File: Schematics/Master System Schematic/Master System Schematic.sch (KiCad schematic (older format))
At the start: 27 parts, among them J1 GND, J2 TS+, J3 TS-, SW1 GLVMS, SW2 SideMounted (BRB), SW3 SideMounted (BRB)

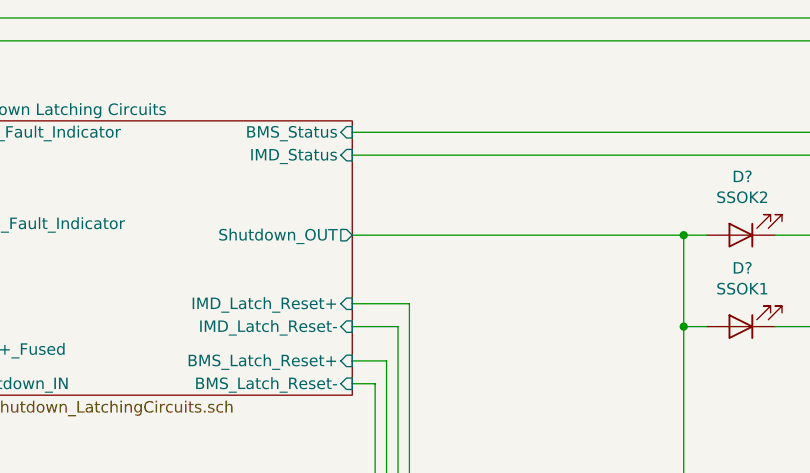
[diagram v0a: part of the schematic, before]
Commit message: Adding ground pin to fault pcb enclosure
Needed ground pin for fault pcb enclosure
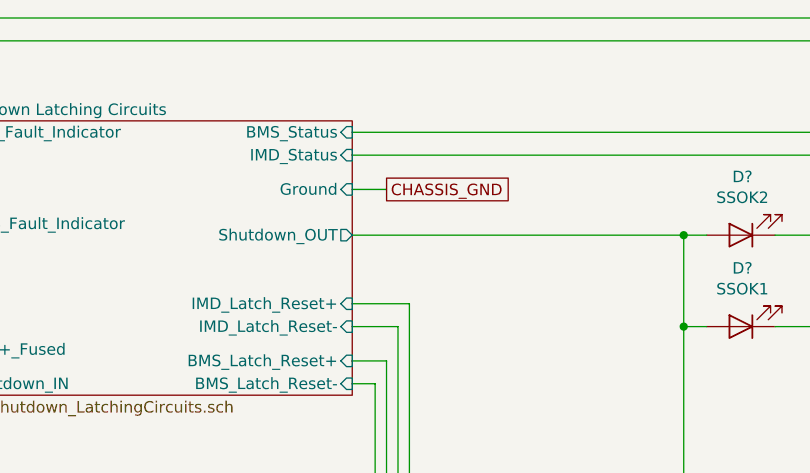
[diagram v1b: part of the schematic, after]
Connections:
- wire segments 140 -> 141
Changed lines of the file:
@@
 F11 "BMS_Latch_Reset+" I R 4700 2500 50
 F12 "BMS_Latch_Reset-" I R 4700 2600 50
+F13 "Ground" I R 4700 1750 50
 $EndSheet
 $Comp
@@
 Wire Wire Line
 	6150 5100 6150 5500
+Text GLabel 4850 1750 2    50   UnSpc ~ 0
+CHASSIS_GND
+Wire Wire Line
+	4850 1750 4700 1750
 $EndSCHEMATC

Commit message: Updated shutdown circuit to reflect changes
>updated latching circuit design to be 4 DPDT relays
>updated reset switch design to be dpst button to actuate both latches simultaneously
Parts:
- removed SW?: IMD_FaultLatch_Reset, symbol Switch:SW_Push
- removed SW?: BMS_FaultLatch_Reset, symbol Switch:SW_Push
- added SW?: Latching Circuit Reset [Momentary Button NO], symbol Switch:SW_DPST
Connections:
- wire segments 141 -> 145
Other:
- moved on the sheet: J1, J2, J3
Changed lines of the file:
@@
 F3 "Shutdown_IN" I L 2950 2600 50
 F4 "IMD_Fault_Indicator" O L 2950 1500 50
-F5 "IMD_Latch_Reset+" I R 4700 2250 50
-F6 "IMD_Latch_Reset-" I R 4700 2350 50
+F5 "IMD_Latch_Reset+" I R 4700 2400 50
+F6 "IMD_Latch_Reset-" I R 4700 2500 50
 F7 "GLV+_Fused" I L 2950 2450 50
 F8 "IMD_Status" I R 4700 1600 50
 F9 "BMS_Status" I R 4700 1500 50
 F10 "BMS_Fault_Indicator" O L 2950 1900 50
-F11 "BMS_Latch_Reset+" I R 4700 2500 50
+F11 "BMS_Latch_Reset+" I R 4700 2300 50
 F12 "BMS_Latch_Reset-" I R 4700 2600 50
 F13 "Ground" I R 4700 1750 50
@@
 L Connector:Conn_01x01_Female J3
 U 1 1 5FB0713A
-P 5550 7950
-F 0 "J3" V 5450 7800 50  0000 L CNN
-F 1 "TS-" V 5350 7750 50  0000 L CNN
-F 2 "" H 5550 7950 50  0001 C CNN
-F 3 "~" H 5550 7950 50  0001 C CNN
-	1    5550 7950
+P 5850 8650
+F 0 "J3" V 5750 8500 50  0000 L CNN
+F 1 "TS-" V 5650 8450 50  0000 L CNN
+F 2 "" H 5850 8650 50  0001 C CNN
+F 3 "~" H 5850 8650 50  0001 C CNN
+	1    5850 8650
 	0    -1   1    0
 $EndComp
@@
 L Connector:Conn_01x01_Female J2
 U 1 1 5FB022E4
-P 5300 7950
-F 0 "J2" V 5200 7800 50  0000 L CNN
-F 1 "TS+" V 5100 7750 50  0000 L CNN
-F 2 "" H 5300 7950 50  0001 C CNN
-F 3 "~" H 5300 7950 50  0001 C CNN
-	1    5300 7950
+P 5600 8650
+F 0 "J2" V 5500 8500 50  0000 L CNN
+F 1 "TS+" V 5400 8450 50  0000 L CNN
+F 2 "" H 5600 8650 50  0001 C CNN
+F 3 "~" H 5600 8650 50  0001 C CNN
+	1    5600 8650
 	0    -1   1    0
 $EndComp
@@
 L Connector:Conn_01x01_Female J1
 U 1 1 5FAE402D
-P 5050 7950
-F 0 "J1" V 4950 7800 50  0000 L CNN
-F 1 "GND" V 4850 7750 50  0000 L CNN
-F 2 "" H 5050 7950 50  0001 C CNN
-F 3 "~" H 5050 7950 50  0001 C CNN
-	1    5050 7950
+P 6100 8650
+F 0 "J1" V 6000 8500 50  0000 L CNN
+F 1 "GND" V 5900 8450 50  0000 L CNN
+F 2 "" H 6100 8650 50  0001 C CNN
+F 3 "~" H 6100 8650 50  0001 C CNN
+	1    6100 8650
 	0    -1   1    0
 $EndComp
-Text Notes 3850 8200 0    50   ~ 0
+Text Notes 4400 8900 0    50   ~ 0
 TSMP and Shutdown Reset Container
 Text GLabel 6150 5600 0    50   UnSpc ~ 0
@@
 F18 "Segment4_VoltageTaps" I L 10100 6850 50
 $EndSheet
-Text GLabel 5150 6750 2    50   UnSpc ~ 0
+Text GLabel 6450 8050 2    50   UnSpc ~ 0
 CHASSIS_GND
 $Comp
@@
 Wire Wire Line
 	1850 1000 1850 3350
-$Comp
-L Switch:SW_Push SW?
-U 1 1 5FA44CBD
-P 4400 7700
-F 0 "SW?" H 4400 7850 50  0000 C CNN
-F 1 "IMD_FaultLatch_Reset" H 4400 7950 50  0000 C CNN
-F 2 "" H 4400 7900 50  0001 C CNN
-F 3 "https://www.mouser.com/datasheet/2/57/Bulgin_2010_p194-10070.pdf" H 4400 7900 50  0001 C CNN
-	1    4400 7700
-	-1   0    0    1
-$EndComp
-$Comp
-L Switch:SW_Push SW?
-U 1 1 5FA470C6
-P 4400 7150
-F 0 "SW?" H 4400 7300 50  0000 C CNN
-F 1 "BMS_FaultLatch_Reset" H 4400 7400 50  0000 C CNN
-F 2 "" H 4400 7350 50  0001 C CNN
-F 3 "https://www.mouser.com/datasheet/2/57/Bulgin_2010_p194-10070.pdf" H 4400 7350 50  0001 C CNN
-	1    4400 7150
-	-1   0    0    1
-$EndComp
 Wire Wire Line
 	6150 5500 6700 5500
@@
 	6150 1950 6250 1950
 Wire Wire Line
-	4600 7700 4950 7700
-Wire Wire Line
-	4200 7700 4000 7700
-Wire Wire Line
-	4000 7700 4000 7600
-Wire Wire Line
-	4000 7600 4900 7600
-Wire Wire Line
-	4200 7150 4000 7150
-Wire Wire Line
-	4000 7150 4000 7050
-Wire Wire Line
-	4600 7150 4850 7150
-Wire Wire Line
-	4000 7050 4800 7050
-Wire Wire Line
-	4800 2600 4700 2600
-Wire Wire Line
-	4700 2500 4850 2500
-Wire Wire Line
-	4900 2350 4700 2350
-Wire Wire Line
-	4700 2250 4950 2250
-Wire Wire Line
 	6150 2350 6150 3150
 Connection ~ 6150 2350
@@
 	6150 4400 6150 3550
 Wire Notes Line
-	3800 8050 3800 6850
+	4350 8750 4350 7550
 Wire Notes Line
-	3800 6850 5850 6850
+	4350 7550 6400 7550
 Wire Notes Line
-	5850 6850 5850 8050
+	6400 7550 6400 8750
 Wire Notes Line
-	5850 8050 3800 8050
+	6400 8750 4350 8750
 Wire Wire Line
 	11500 6100 11700 6100
@@
 $EndComp
 Wire Wire Line
-	5150 6750 5050 6750
-Wire Wire Line
-	5300 7100 6700 7100
-Wire Wire Line
-	5550 7200 6700 7200
-Wire Wire Line
-	4800 2600 4800 7050
-Wire Wire Line
-	4850 2500 4850 7150
-Wire Wire Line
-	4900 2350 4900 7600
-Wire Wire Line
-	4950 2250 4950 7700
-Wire Wire Line
 	1850 3950 6900 3950
 Wire Wire Line
@@
 Wire Wire Line
 	2300 2600 2300 3000
-Wire Wire Line
-	5050 6750 5050 7750
-Wire Wire Line
-	5300 7100 5300 7750
-Wire Wire Line
-	5550 7200 5550 7750
 Connection ~ 6150 5100
 Wire Wire Line
@@
 Wire Wire Line
 	4850 1750 4700 1750
+Wire Wire Line
+	4750 8150 4700 8150
+Wire Wire Line
+	4700 8150 4700 8050
+Wire Wire Line
+	4700 8050 4900 8050
+Wire Wire Line
+	5150 8150 5200 8150
+Wire Wire Line
+	5200 8150 5200 8050
+Wire Wire Line
+	5200 8050 5000 8050
+Wire Wire Line
+	5150 8350 5250 8350
+Wire Wire Line
+	5250 8350 5250 8000
+Wire Wire Line
+	5250 8000 5050 8000
+Wire Wire Line
+	4750 8350 4650 8350
+Wire Wire Line
+	4650 8350 4650 8000
+Wire Wire Line
+	4650 8000 4850 8000
+Wire Wire Line
+	4850 2600 4850 8000
+Wire Wire Line
+	5050 2300 4700 2300
+Wire Wire Line
+	4700 2600 4850 2600
+Wire Wire Line
+	5050 2300 5050 8000
+Wire Wire Line
+	4700 2400 5000 2400
+Wire Wire Line
+	5000 2400 5000 8050
+Wire Wire Line
+	4900 2500 4700 2500
+Wire Wire Line
+	4900 2500 4900 8050
+Wire Wire Line
+	6700 7100 5600 7100
+Wire Wire Line
+	5600 7100 5600 8450
+Wire Wire Line
+	5850 7200 6700 7200
+Wire Wire Line
+	5850 7200 5850 8450
+Wire Wire Line
+	6450 8050 6100 8050
+Wire Wire Line
+	6100 8050 6100 8450
+$Comp
+L Switch:SW_DPST SW?
+U 1 1 5F864268
+P 4950 8250
+F 0 "SW?" H 4950 8050 50  0000 C CNN
+F 1 "Latching Circuit Reset [Momentary Button NO]" H 4500 7900 50  0000 C CNN
+F 2 "" H 4950 8250 50  0001 C CNN
+F 3 "~" H 4950 8250 50  0001 C CNN
+	1    4950 8250
+	1    0    0    -1
+$EndComp
 $EndSCHEMATC

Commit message: Add CAN Bus Module to Pedal Box
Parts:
- added A1: Arduino_UNO_rev3, symbol NER:Arduino_UNO_rev3
- added R? (x2): R, symbol Device:R
- added U1: CAN_Module, symbol NER:CAN-Module
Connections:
- net labels added: CAN_H, CAN_L, GLV+, GLV_GND, POT1+, POT1-, POT1_INPUT, POT2+, POT2-, POT2_INPUT, Switch1-, Switch2-, Switch_Input1, Switch_Input2
- wire segments 145 -> 205
- no-connect marks 0 -> 26
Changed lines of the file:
@@
 $Descr B 17000 11000
 encoding utf-8
-Sheet 1 11
+Sheet 1 12
 Title "NER FH 2020-2021 Master Electrical Schematic"
 Date "2020-09-17"
@@
 $EndComp
 Wire Wire Line
-	1850 3950 6900 3950
-Wire Wire Line
 	4700 1950 6150 1950
 Wire Wire Line
@@
 	2300 2600 2300 3000
 Connection ~ 6150 5100
-Wire Wire Line
-	6150 5100 6150 5500
 Text GLabel 4850 1750 2    50   UnSpc ~ 0
 CHASSIS_GND
@@
 	1    0    0    -1
 $EndComp
+Text HLabel 6600 3050 2    50   Input ~ 0
+GLV+
+Wire Wire Line
+	6600 3050 5550 3050
+Text HLabel 3600 3050 0    50   Input ~ 0
+GLV_GND
+Wire Wire Line
+	3600 3050 4350 3050
+$Comp
+L NER:Arduino_UNO_rev3 A1
+U 1 1 5F6833F8
+P 4950 2900
+F 0 "A1" H 4950 3015 50  0000 C CNN
+F 1 "Arduino_UNO_rev3" H 4950 2924 50  0000 C CNN
+F 2 "" H 4950 3050 50  0001 C CNN
+F 3 "" H 4950 3050 50  0001 C CNN
+	1    4950 2900
+	1    0    0    -1
+$EndComp
+$Comp
+L NER:CAN-Module U1
+U 1 1 5F6A22C3
+P 7600 3100
+F 0 "U1" H 7625 3115 50  0000 C CNN
+F 1 "CAN_Module" H 7625 3024 50  0000 C CNN
+F 2 "" H 7600 3100 50  0001 C CNN
+F 3 "" H 7600 3100 50  0001 C CNN
+	1    7600 3100
+	1    0    0    -1
+$EndComp
+Wire Wire Line
+	7050 3450 5900 3450
+Wire Wire Line
+	5900 3450 5900 3650
+Wire Wire Line
+	5900 3650 5550 3650
+Wire Wire Line
+	7050 3550 6100 3550
+Wire Wire Line
+	6100 3550 6100 3850
+Wire Wire Line
+	6100 3850 5550 3850
+Wire Wire Line
+	7050 3650 6250 3650
+Wire Wire Line
+	6250 3650 6250 3750
+Wire Wire Line
+	6250 3750 5550 3750
+Wire Wire Line
+	7050 3750 6350 3750
+Wire Wire Line
+	6350 3750 6350 3950
+Wire Wire Line
+	7050 3850 6600 3850
+Wire Wire Line
+	6600 3850 6600 3400
+Wire Wire Line
+	6600 3400 5750 3400
+Wire Wire Line
+	5750 3400 5750 3550
+Wire Wire Line
+	5750 3550 5550 3550
+Text HLabel 8950 3650 2    50   Input ~ 0
+CAN_L
+Text HLabel 8950 3500 2    50   Input ~ 0
+CAN_H
+Wire Wire Line
+	8200 3500 8600 3500
+Wire Wire Line
+	8950 3650 8200 3650
+NoConn ~ 4350 3200
+NoConn ~ 4350 3300
+NoConn ~ 4350 3400
+NoConn ~ 4350 3500
+Wire Wire Line
+	5550 4700 5900 4700
+Wire Wire Line
+	5900 4700 5900 4900
+Connection ~ 5900 4700
+$Comp
+L Device:R R?
+U 1 1 5F71A5F5
+P 5900 5050
+F 0 "R?" H 5970 5096 50  0000 L CNN
+F 1 "R" H 5970 5005 50  0000 L CNN
+F 2 "" V 5830 5050 50  0001 C CNN
+F 3 "~" H 5900 5050 50  0001 C CNN
+	1    5900 5050
+	1    0    0    -1
+$EndComp
+$Comp
+L Device:R R?
+U 1 1 5F71A986
+P 6150 5050
+F 0 "R?" H 6220 5096 50  0000 L CNN
+F 1 "R" H 6220 5005 50  0000 L CNN
+F 2 "" V 6080 5050 50  0001 C CNN
+F 3 "~" H 6150 5050 50  0001 C CNN
+	1    6150 5050
+	1    0    0    -1
+$EndComp
+Wire Wire Line
+	5900 5200 5900 5400
+Wire Wire Line
+	5900 5400 6000 5400
+NoConn ~ 7050 3350
+NoConn ~ 5550 3250
+NoConn ~ 5550 3350
+NoConn ~ 5550 3450
+NoConn ~ 4350 3650
+NoConn ~ 4350 3750
+NoConn ~ 4350 3850
+NoConn ~ 4350 3950
+NoConn ~ 4350 4350
+NoConn ~ 4350 4700
+NoConn ~ 4350 4800
+NoConn ~ 4350 4900
+NoConn ~ 4350 5000
+NoConn ~ 5550 5000
+NoConn ~ 5550 4900
+NoConn ~ 5550 4600
+NoConn ~ 5550 4500
+NoConn ~ 5550 4400
+NoConn ~ 5550 4300
+NoConn ~ 5550 4150
+NoConn ~ 5550 4050
+Text HLabel 6800 4700 2    50   Input ~ 0
+Switch_Input1
+Text HLabel 6800 5050 2    50   Input ~ 0
+Switch_Input2
+Wire Wire Line
+	4350 4250 3950 4250
+Wire Wire Line
+	3950 4250 3950 4600
+Wire Wire Line
+	3950 5650 6000 5650
+Wire Wire Line
+	6600 5650 6600 5150
+Wire Wire Line
+	6600 4600 6800 4600
+Wire Wire Line
+	5900 4700 6800 4700
+Wire Wire Line
+	6150 4900 6150 4800
+Wire Wire Line
+	5550 4800 6150 4800
+Wire Wire Line
+	6150 4800 6400 4800
+Wire Wire Line
+	6400 4800 6400 5050
+Wire Wire Line
+	6400 5050 6800 5050
+Connection ~ 6150 4800
+Wire Wire Line
+	6600 5150 6800 5150
+Connection ~ 6600 5150
+Wire Wire Line
+	6600 5150 6600 4600
+Text HLabel 6800 5150 2    50   Input ~ 0
+Switch2-
+Text HLabel 6800 4600 2    50   Input ~ 0
+Switch1-
+Wire Wire Line
+	4350 4500 3300 4500
+Wire Wire Line
+	3950 4600 3300 4600
+Connection ~ 3950 4600
+Wire Wire Line
+	3950 4600 3950 5100
+Wire Wire Line
+	4350 4600 4150 4600
+Wire Wire Line
+	4150 4600 4150 5000
+Wire Wire Line
+	4350 4050 3850 4050
+Wire Wire Line
+	3850 4050 3850 4400
+Wire Wire Line
+	3850 4400 3300 4400
+Wire Wire Line
+	3850 4400 3850 4900
+Wire Wire Line
+	3850 4900 3300 4900
+Connection ~ 3850 4400
+Wire Wire Line
+	3950 5100 3300 5100
+Connection ~ 3950 5100
+Wire Wire Line
+	3950 5100 3950 5650
+Text HLabel 3300 4400 0    50   Input ~ 0
+POT1+
+Text HLabel 3300 4900 0    50   Input ~ 0
+POT2+
+Text HLabel 3300 4500 0    50   Input ~ 0
+POT1_INPUT
+Text HLabel 3300 4600 0    50   Input ~ 0
+POT1-
+Wire Wire Line
+	4150 5000 3300 5000
+Text HLabel 3300 5000 0    50   Input ~ 0
+POT2_INPUT
+Text HLabel 3300 5100 0    50   Input ~ 0
+POT2-
+Wire Wire Line
+	7050 3950 7050 4300
+Wire Wire Line
+	7050 4300 7600 4300
+Wire Wire Line
+	7600 4300 7600 5850
+Wire Wire Line
+	7600 5850 2500 5850
+Wire Wire Line
+	2500 5850 2500 4050
+Wire Wire Line
+	2500 4050 3850 4050
+Connection ~ 3850 4050
+Wire Wire Line
+	6000 5400 6000 5650
+Connection ~ 6000 5400
+Wire Wire Line
+	6000 5400 6150 5400
+Connection ~ 6000 5650
+Wire Wire Line
+	6000 5650 6600 5650
+NoConn ~ 4350 4150
+$Sheet
+S 12950 3000 1450 1400
+U 5F6C8190
+F0 "Pedal Box" 50
+F1 "PedalBox.sch" 50
+$EndSheet
+Wire Wire Line
+	8600 3500 8950 3500
+Wire Wire Line
+	1850 3950 6900 3950
+Wire Wire Line
+	6150 5100 6150 5500
 $EndSCHEMATC

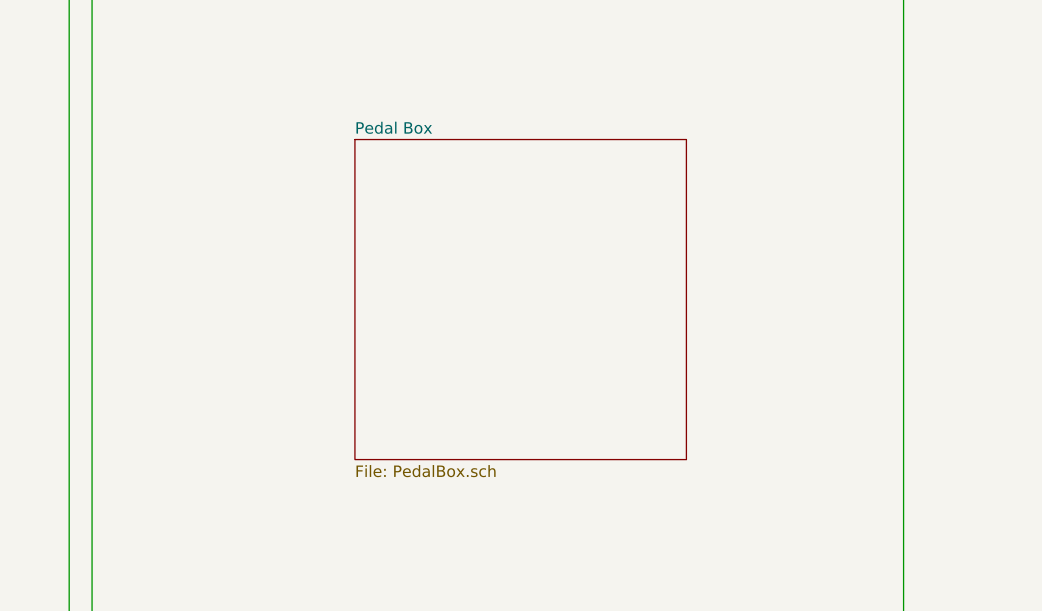
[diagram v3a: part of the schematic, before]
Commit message: Added pedal box sub-schematic to master
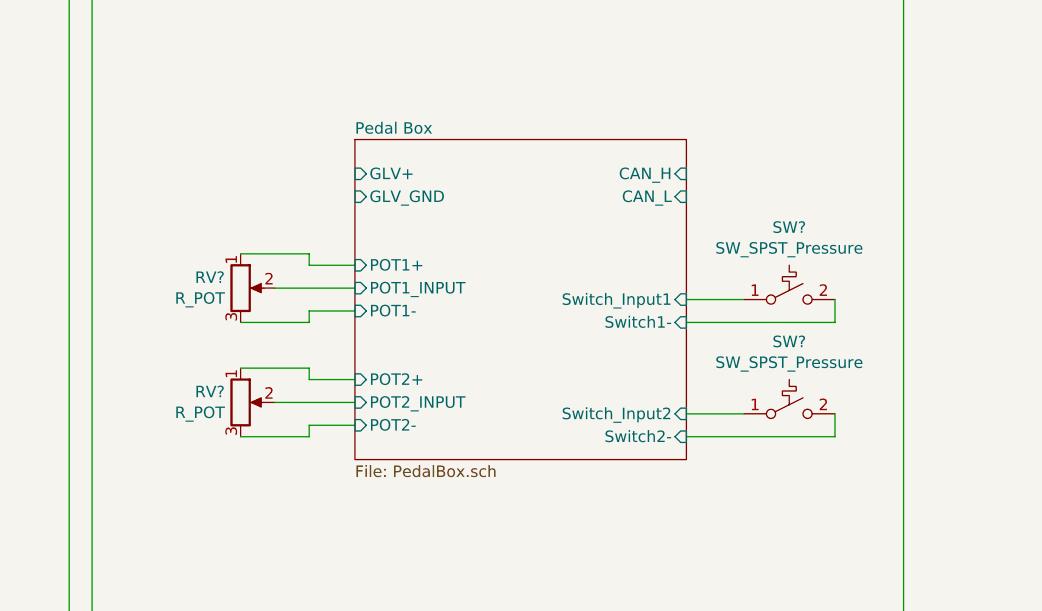
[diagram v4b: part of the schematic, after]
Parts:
- added RV? (x2): R_POT, symbol Device:R_POT
- added SW? (x2): SW_SPST_Pressure, symbol Switch:SW_SPST_Temperature
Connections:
- wire segments 205 -> 225
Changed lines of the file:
@@
 	6000 5650 6600 5650
 NoConn ~ 4350 4150
-$Sheet
-S 12950 3000 1450 1400
-U 5F6C8190
-F0 "Pedal Box" 50
-F1 "PedalBox.sch" 50
-$EndSheet
 Wire Wire Line
 	8600 3500 8950 3500
@@
 Wire Wire Line
 	6150 5100 6150 5500
+$Comp
+L Switch:SW_SPST_Temperature SW?
+U 1 1 5F6E407C
+P 14850 3700
+F 0 "SW?" H 14850 4015 50  0000 C CNN
+F 1 "SW_SPST_Pressure" H 14850 3924 50  0000 C CNN
+F 2 "" H 14850 3700 50  0001 C CNN
+F 3 "~" H 14850 3700 50  0001 C CNN
+	1    14850 3700
+	1    0    0    -1
+$EndComp
+$Comp
+L Switch:SW_SPST_Temperature SW?
+U 1 1 5F6E49B5
+P 14850 4200
+F 0 "SW?" H 14850 4515 50  0000 C CNN
+F 1 "SW_SPST_Pressure" H 14850 4424 50  0000 C CNN
+F 2 "" H 14850 4200 50  0001 C CNN
+F 3 "~" H 14850 4200 50  0001 C CNN
+	1    14850 4200
+	1    0    0    -1
+$EndComp
+Wire Wire Line
+	14400 3700 14650 3700
+Wire Wire Line
+	15050 3700 15050 3800
+Wire Wire Line
+	15050 3800 14400 3800
+Wire Wire Line
+	14400 4200 14650 4200
+Wire Wire Line
+	15050 4200 15050 4300
+Wire Wire Line
+	15050 4300 14400 4300
+$Sheet
+S 12950 3000 1450 1400
+U 5F6C8190
+F0 "Pedal Box" 50
+F1 "PedalBox.sch" 50
+F2 "GLV+" I L 12950 3150 50
+F3 "GLV_GND" I L 12950 3250 50
+F4 "CAN_L" I R 14400 3250 50
+F5 "CAN_H" I R 14400 3150 50
+F6 "Switch_Input1" I R 14400 3700 50
+F7 "Switch_Input2" I R 14400 4200 50
+F8 "Switch2-" I R 14400 4300 50
+F9 "Switch1-" I R 14400 3800 50
+F10 "POT1+" I L 12950 3550 50
+F11 "POT2+" I L 12950 4050 50
+F12 "POT1_INPUT" I L 12950 3650 50
+F13 "POT1-" I L 12950 3750 50
+F14 "POT2_INPUT" I L 12950 4150 50
+F15 "POT2-" I L 12950 4250 50
+$EndSheet
+$Comp
+L Device:R_POT RV?
+U 1 1 5F71DF92
+P 12450 4150
+F 0 "RV?" H 12381 4196 50  0000 R CNN
+F 1 "R_POT" H 12381 4105 50  0000 R CNN
+F 2 "" H 12450 4150 50  0001 C CNN
+F 3 "~" H 12450 4150 50  0001 C CNN
+	1    12450 4150
+	1    0    0    -1
+$EndComp
+$Comp
+L Device:R_POT RV?
+U 1 1 5F71E67B
+P 12450 3650
+F 0 "RV?" H 12381 3696 50  0000 R CNN
+F 1 "R_POT" H 12381 3605 50  0000 R CNN
+F 2 "" H 12450 3650 50  0001 C CNN
+F 3 "~" H 12450 3650 50  0001 C CNN
+	1    12450 3650
+	1    0    0    -1
+$EndComp
+Wire Wire Line
+	12600 3650 12950 3650
+Wire Wire Line
+	12450 3500 12750 3500
+Wire Wire Line
+	12750 3500 12750 3550
+Wire Wire Line
+	12750 3550 12950 3550
+Wire Wire Line
+	12450 3800 12750 3800
+Wire Wire Line
+	12750 3800 12750 3750
+Wire Wire Line
+	12750 3750 12950 3750
+Wire Wire Line
+	12600 4150 12950 4150
+Wire Wire Line
+	12450 4000 12750 4000
+Wire Wire Line
+	12750 4000 12750 4050
+Wire Wire Line
+	12750 4050 12950 4050
+Wire Wire Line
+	12450 4300 12750 4300
+Wire Wire Line
+	12750 4300 12750 4250
+Wire Wire Line
+	12750 4250 12950 4250
 $EndSCHEMATC
